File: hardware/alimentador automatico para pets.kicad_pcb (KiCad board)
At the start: 2 copper layers, 1 part, among them U1 ESP32-DEVKIT-V1

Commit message: pcb design start
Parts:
- added C1: 100n, Capacitor_THT:C_Disc_D6.0mm_W2.5mm_P5.00mm, F.Cu at (94.5, 80.0)
- added C2: 220u, Capacitor_THT:CP_Radial_D8.0mm_P2.50mm, F.Cu at (93.0, 71.0)
- added D1: LED, LED_THT:LED_D3.0mm, B.Cu at (92.0, 99.5)
- added D2: 3V6, Diode_THT:D_DO-35_SOD27_P7.62mm_Horizontal, B.Cu at (111.8, 40.4)
- added J1: Conn_01x02, Connector_PinSocket_2.54mm:PinSocket_1x02_P2.54mm_Vertical, F.Cu at (78.0, 47.0)
- added J2: Conn_01x04, Connector_PinSocket_2.54mm:PinSocket_1x04_P2.54mm_Vertical, F.Cu at (134.6, 77.2)
- added J3: Conn_01x03, Connector_PinSocket_2.54mm:PinSocket_1x03_P2.54mm_Vertical, F.Cu at (95.0, 92.0)
- added J4: Conn_01x03, Connector_PinSocket_2.54mm:PinSocket_1x03_P2.54mm_Vertical, F.Cu at (78.0, 82.0)
- added J5: Conn_01x02, Connector_PinSocket_2.54mm:PinSocket_1x02_P2.54mm_Vertical, F.Cu at (78.0, 38.0)
- added J6: Conn_01x05, Connector_PinSocket_2.54mm:PinSocket_1x05_P2.54mm_Vertical, F.Cu at (138.8, 35.4)
- added J7: Conn_01x02, Connector_PinSocket_2.54mm:PinSocket_1x02_P2.54mm_Vertical, F.Cu at (139.0, 66.0)
- added J8: Conn_01x04, Connector_PinSocket_2.54mm:PinSocket_1x04_P2.54mm_Vertical, F.Cu at (139.0, 51.9)
- added PS1: HLK-PM01 5V, Converter_ACDC:Converter_ACDC_HiLink_HLK-PMxx, F.Cu at (94.5, 32.4)
- added R1: 10k, Resistor_THT:R_Axial_DIN0207_L6.3mm_D2.5mm_P7.62mm_Horizontal, F.Cu at (82.2, 87.0)
- added R2: 10k, Resistor_THT:R_Axial_DIN0207_L6.3mm_D2.5mm_P7.62mm_Horizontal, F.Cu at (85.8, 71.0)
- added R3: 4k7, Resistor_THT:R_Axial_DIN0207_L6.3mm_D2.5mm_P7.62mm_Horizontal, F.Cu at (78.0, 68.0)
- added R4: 470, Resistor_THT:R_Axial_DIN0207_L6.3mm_D2.5mm_P7.62mm_Horizontal, B.Cu at (78.0, 87.2)
- added R5: 470, Resistor_THT:R_Axial_DIN0207_L6.3mm_D2.5mm_P7.62mm_Horizontal, B.Cu at (125.8, 58.4)
- added R6: 10k, Resistor_THT:R_Axial_DIN0207_L6.3mm_D2.5mm_P7.62mm_Horizontal, F.Cu at (90.0, 92.0)
- added SW1: SW_Push, Button_Switch_THT:SW_PUSH_6mm, B.Cu at (118.8, 97.8)
- added SW2: SW_Push, Button_Switch_THT:SW_PUSH_6mm, B.Cu at (130.8, 97.5)
- added SW3: SW_Push, Button_Switch_THT:SW_PUSH_6mm, B.Cu at (106.2, 97.5)
- added U2: HX711_module, footprint_lib:HX711_module, F.Cu at (114.2, 83.2)
- moved U1 49.5 mm to (119.4, 46.0)
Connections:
- net Net-(U1-Pad2) renamed GND
- U1 pad 1: unconnected-(U1-Pad1) -> /3V3
- U1 pad 10: unconnected-(U1-Pad10) -> /sMotor
- U1 pad 11: unconnected-(U1-Pad11) -> /SDA_disp
- U1 pad 14: unconnected-(U1-Pad14) -> /SCL_disp
- U1 pad 19: unconnected-(U1-Pad19) -> /led_on
- U1 pad 21: unconnected-(U1-Pad21) -> /BUTTON_1
- U1 pad 22: unconnected-(U1-Pad22) -> /BUTTON_2
- U1 pad 23: unconnected-(U1-Pad23) -> /BUTTON_3
- U1 pad 25: unconnected-(U1-Pad25) -> /SCK
- U1 pad 26: unconnected-(U1-Pad26) -> /DT_encoder
- U1 pad 27: unconnected-(U1-Pad27) -> /DT
- U1 pad 28: unconnected-(U1-Pad28) -> /SW_encoder
- U1 pad 3: unconnected-(U1-Pad3) -> /CLK_encoder
- U1 pad 30: unconnected-(U1-Pad30) -> /5V
- U1 pad 5: unconnected-(U1-Pad5) -> /IR_out
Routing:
- net GND: vias 0 -> 4
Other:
- board outline added: 69.5 x 88 mm

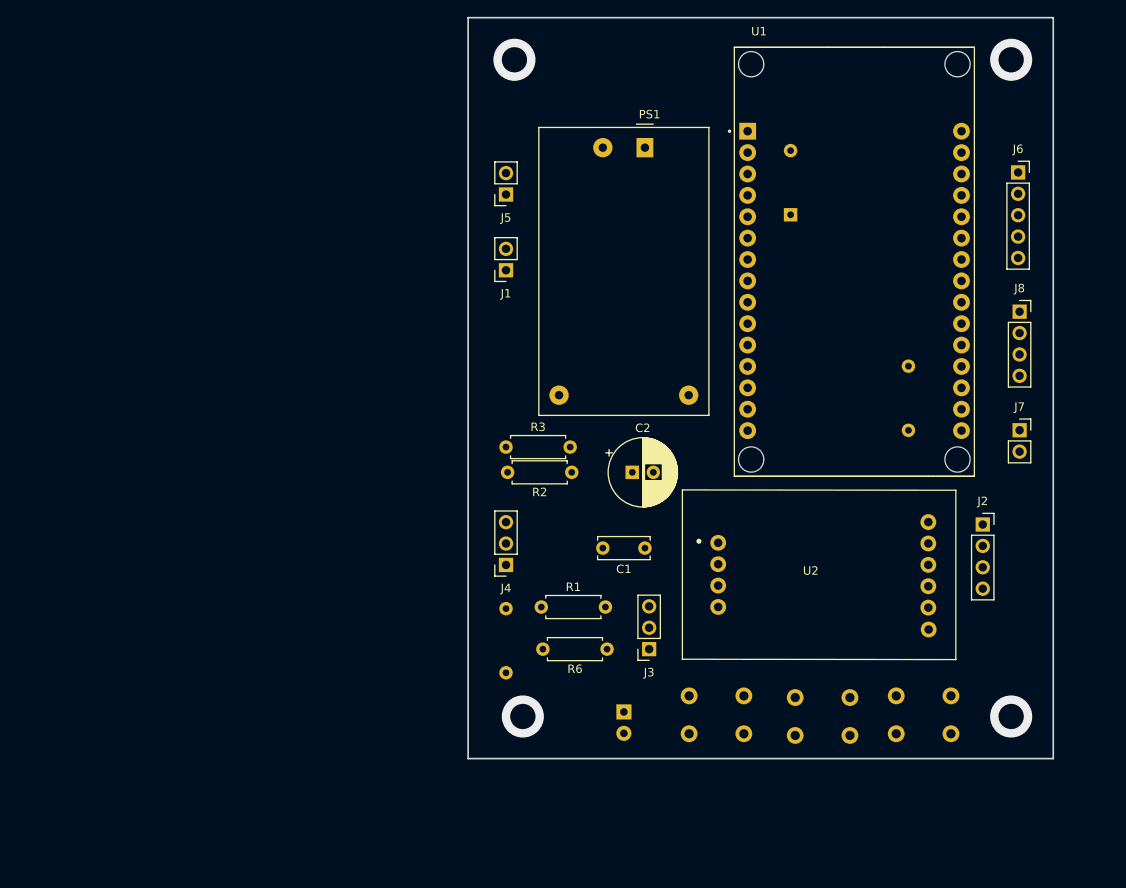
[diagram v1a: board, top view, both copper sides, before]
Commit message: removing leds and changing components positions #14
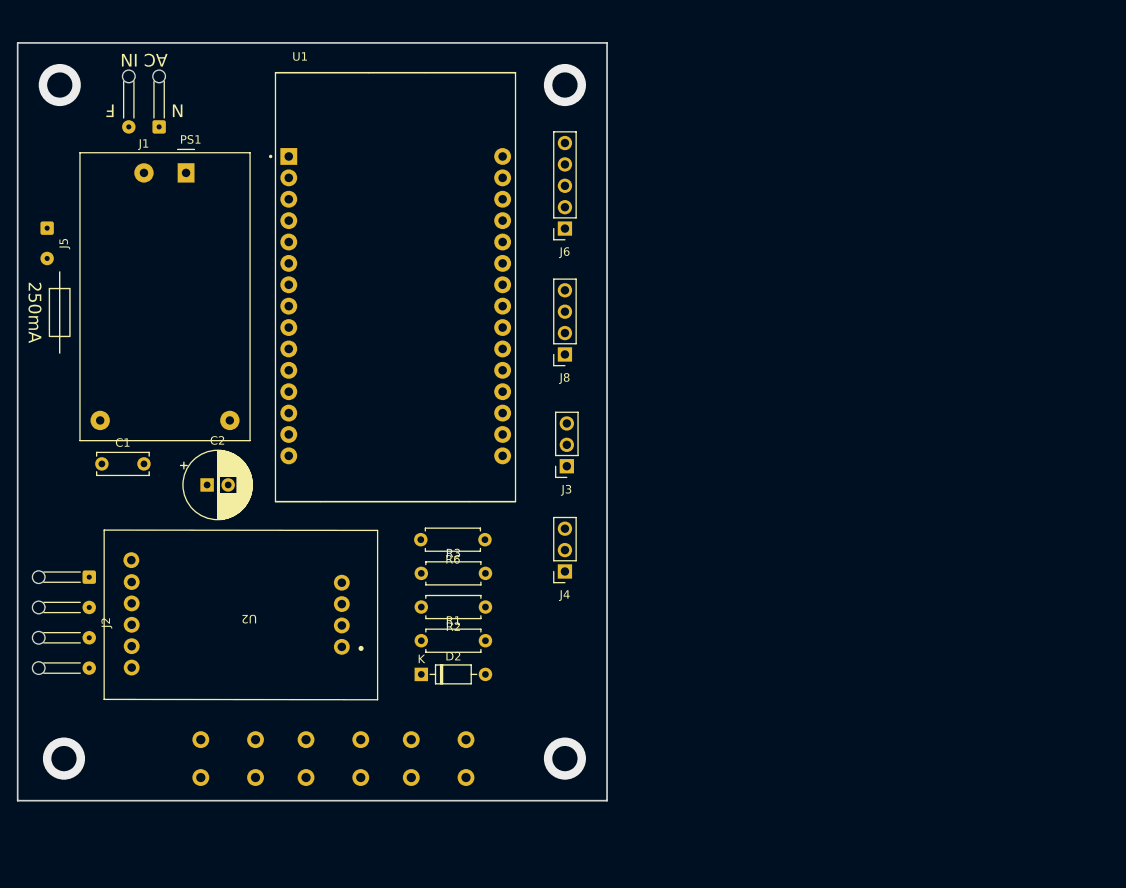
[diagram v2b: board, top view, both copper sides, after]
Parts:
- removed D1: LED, LED_THT:LED_D3.0mm
- removed J7: Conn_01x02, Connector_PinSocket_2.54mm:PinSocket_1x02_P2.54mm_Vertical
- removed R4, R5: 470, Resistor_THT:R_Axial_DIN0207_L6.3mm_D2.5mm_P7.62mm_Horizontal
- added G***: LOGO, footprint_lib:fuse_ieee, F.Cu at (25.0, 52.0)
- D2: moved to F.Cu
- J1: footprint Connector_PinSocket_2.54mm:PinSocket_1x02_P2.54mm_Vertical -> Connector_Wire:SolderWire-0.1sqmm_1x02_P3.6mm_D0.4mm_OD1mm_Relief
- J2: footprint Connector_PinSocket_2.54mm:PinSocket_1x04_P2.54mm_Vertical -> Connector_Wire:SolderWire-0.1sqmm_1x04_P3.6mm_D0.4mm_OD1mm_Relief
- J5: footprint Connector_PinSocket_2.54mm:PinSocket_1x02_P2.54mm_Vertical -> Connector_Wire:SolderWire-0.1sqmm_1x02_P3.6mm_D0.4mm_OD1mm
- moved J2 106.3 mm to (28.5, 83.5), turned to -90 degrees
- moved D2 70.0 mm to (67.9, 95.0), turned to 0 degrees
- moved U2 66.9 mm to (47.5, 87.9), turned to 180 degrees
- moved C1 65.3 mm to (30.0, 70.0), turned to 0 degrees
- moved SW1 58.3 mm to (60.8, 102.8)
- moved SW3 58.2 mm to (48.2, 102.8)
- moved SW2 57.8 mm to (73.2, 102.8)
- moved J5 54.6 mm to (23.5, 42.0), turned to -90 degrees
- moved PS1 54.6 mm to (40.0, 35.4)
- moved U1 54.6 mm to (64.9, 49.0)
- moved J8 54.2 mm to (85.0, 57.0), turned to 180 degrees
- moved J6 54.2 mm to (85.0, 42.0), turned to 180 degrees
- moved C2 50.5 mm to (42.5, 72.5)
- moved J1 44.6 mm to (36.8, 30.0)
- moved J3 23.8 mm to (85.2, 70.3)
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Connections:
- J2 pad 1: /red_wire -> /green_wire
- J2 pad 2: /black_wire -> /white_wire
- J2 pad 3: /white_wire -> /black_wire
- J2 pad 4: /green_wire -> /red_wire
- J3 pad 2: /5V -> GND
- J3 pad 3: GND -> /5V
- J6 pad 1: /CLK_encoder -> GND
- J6 pad 2: /DT_encoder -> /3V3
- J6 pad 4: /3V3 -> /DT_encoder
- J6 pad 5: GND -> /CLK_encoder
- J8 pad 1: /SCL_disp -> GND
- J8 pad 2: /SDA_disp -> /5V
- J8 pad 3: /5V -> /SDA_disp
- J8 pad 4: GND -> /SCL_disp
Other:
- board size 69.5 x 88 mm -> 70 x 90 mm
- board text added: "250mA"
- board text added: "AC IN"
- board text added: "F"
- board text added: "N"

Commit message: add battery module
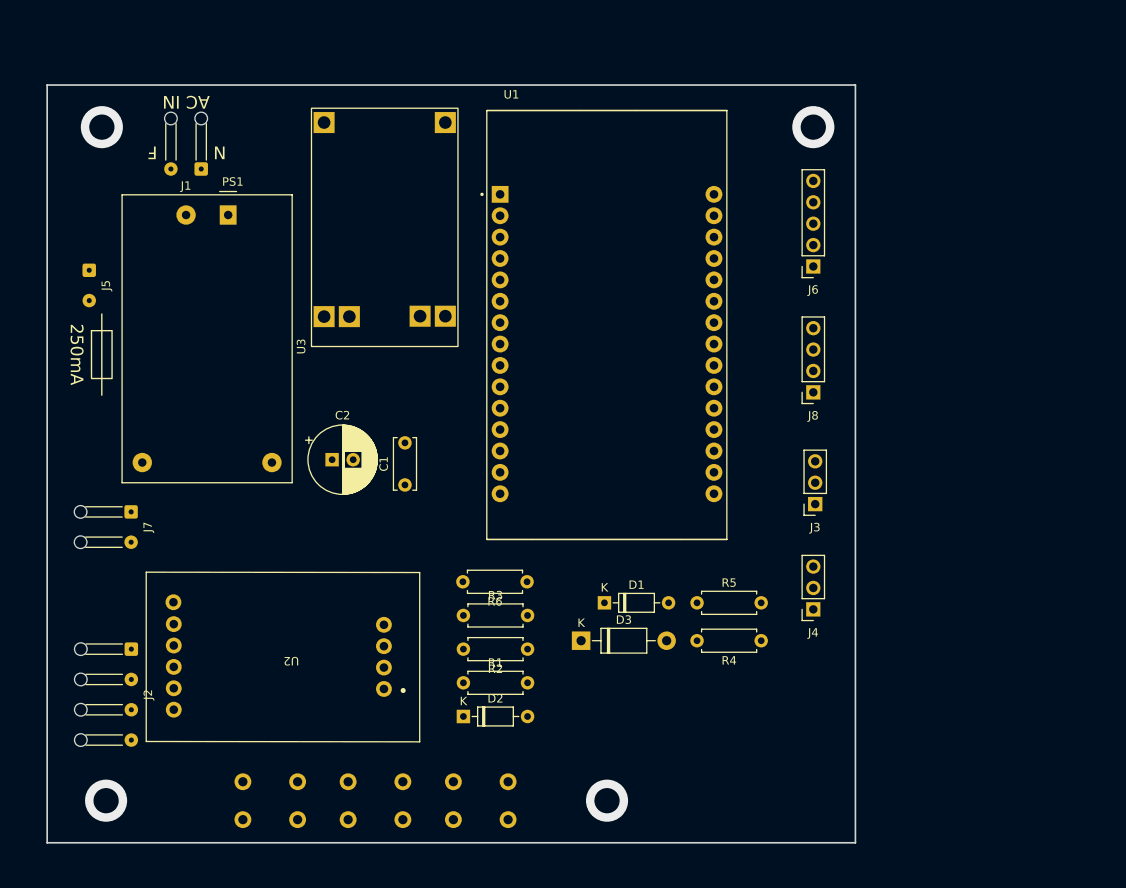
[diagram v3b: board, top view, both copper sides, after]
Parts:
- added D1: 3V6, Diode_THT:D_DO-35_SOD27_P7.62mm_Horizontal, F.Cu at (89.7, 86.5)
- added D3: 1N4007, Diode_THT:D_DO-41_SOD81_P10.16mm_Horizontal, F.Cu at (86.9, 91.0)
- added J7: Conn_01x02, Connector_Wire:SolderWire-0.1sqmm_1x02_P3.6mm_D0.4mm_OD1mm_Relief, F.Cu at (33.5, 75.7)
- added R4: 10k, Resistor_THT:R_Axial_DIN0207_L6.3mm_D2.5mm_P7.62mm_Horizontal, F.Cu at (108.3, 91.0)
- added R5: 10k, Resistor_THT:R_Axial_DIN0207_L6.3mm_D2.5mm_P7.62mm_Horizontal, F.Cu at (100.7, 86.5)
- added U3: TP4056, footprint_lib:TP4056, F.Cu at (54.9, 56.1)
- R3: value 4k7 -> 10k
- moved C1 36.1 mm to (66.0, 72.5), turned to 90 degrees
- moved J3 29.8 mm to (114.7, 74.8)
- moved J4 29.8 mm to (114.5, 87.3)
- moved J6 29.8 mm to (114.5, 46.5)
- moved J8 29.8 mm to (114.5, 61.5)
- moved U1 25.5 mm to (90.0, 53.5)
- moved C2 15.1 mm to (57.3, 69.5)
- moved J2 9.90 mm to (33.5, 92.0)
- moved D2 7.07 mm to (72.9, 100.0)
- moved G*** 7.07 mm to (30.0, 57.0)
- moved J1 7.07 mm to (41.8, 35.0)
- moved J5 7.07 mm to (28.5, 47.0)
- moved PS1 7.07 mm to (45.0, 40.4)
- moved R1 7.07 mm to (72.9, 96.0)
- moved R2 7.07 mm to (80.6, 92.0)
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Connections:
- R2 pad 2: Net-(R2-Pad2) -> Net-(R1-Pad2)
- R3 pad 1: Net-(R2-Pad2) -> /5V
- R3 pad 2: Net-(R1-Pad2) -> Net-(R3-Pad2)
- U1 pad 24: unconnected-(U1-Pad24) -> /ac_check
- U1 pad 30: /5V -> /+Vcc
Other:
- board size 70 x 90 mm -> 96 x 90 mm

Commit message: att schematic #14
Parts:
- J4: footprint Connector_PinSocket_2.54mm:PinSocket_1x03_P2.54mm_Vertical -> Connector_PinHeader_2.54mm:PinHeader_1x03_P2.54mm_Vertical
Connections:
- J4 pad 1: /5V -> /sMotor
- J4 pad 2: /sMotor -> /5V
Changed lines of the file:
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@@
     )
   )
-  (footprint "Connector_PinSocket_2.54mm:PinSocket_1x03_P2.54mm_Vertical" (layer "F.Cu")
+  (footprint "Connector_PinHeader_2.54mm:PinHeader_1x03_P2.54mm_Vertical" (layer "F.Cu")
     (at 114.5 87.275 180)
-    (descr "Through hole straight socket strip, 1x03, 2.54mm pitch, single row (from Kicad 4.0.7), script generated")
-    (tags "Through hole socket strip THT 1x03 2.54mm single row")
+    (descr "Through hole straight pin header, 1x03, 2.54mm pitch, single row")
+    (tags "Through hole pin header THT 1x03 2.54mm single row")
     (property "Sheetfile" "alimentador automatico para pets.kicad_sch")
     (property "Sheetname" "")
     (attr through_hole)
-    (fp_text reference "J4" (at 0 -2.77 180) (layer "F.SilkS")
+    (fp_text reference "J4" (at 0 -2.33 180) (layer "F.SilkS")
       (effects (font (size 1 1) (thickness 0.15)))
     )
-    (fp_text value "Conn_01x03" (at 0 7.85 180) (layer "F.Fab")
+    (fp_text value "Conn_01x03" (at 0 7.41 180) (layer "F.Fab")
       (effects (font (size 1 1) (thickness 0.15)))
     )
@@
     )
     (fp_line (start 1.33 1.27) (end 1.33 6.41) (layer "F.SilkS") (width 0.12))
-    (fp_line (start 0 -1.33) (end 1.33 -1.33) (layer "F.SilkS") (width 0.12))
+    (fp_line (start -1.33 0) (end -1.33 -1.33) (layer "F.SilkS") (width 0.12))
+    (fp_line (start -1.33 6.41) (end 1.33 6.41) (layer "F.SilkS") (width 0.12))
     (fp_line (start -1.33 1.27) (end 1.33 1.27) (layer "F.SilkS") (width 0.12))
-    (fp_line (start -1.33 6.41) (end 1.33 6.41) (layer "F.SilkS") (width 0.12))
+    (fp_line (start -1.33 -1.33) (end 0 -1.33) (layer "F.SilkS") (width 0.12))
     (fp_line (start -1.33 1.27) (end -1.33 6.41) (layer "F.SilkS") (width 0.12))
-    (fp_line (start 1.33 -1.33) (end 1.33 0) (layer "F.SilkS") (width 0.12))
-    (fp_line (start 1.75 6.85) (end -1.8 6.85) (layer "F.CrtYd") (width 0.05))
-    (fp_line (start -1.8 -1.8) (end 1.75 -1.8) (layer "F.CrtYd") (width 0.05))
-    (fp_line (start 1.75 -1.8) (end 1.75 6.85) (layer "F.CrtYd") (width 0.05))
-    (fp_line (start -1.8 6.85) (end -1.8 -1.8) (layer "F.CrtYd") (width 0.05))
-    (fp_line (start -1.27 -1.27) (end 0.635 -1.27) (layer "F.Fab") (width 0.1))
+    (fp_line (start -1.8 -1.8) (end -1.8 6.85) (layer "F.CrtYd") (width 0.05))
+    (fp_line (start 1.8 6.85) (end 1.8 -1.8) (layer "F.CrtYd") (width 0.05))
+    (fp_line (start 1.8 -1.8) (end -1.8 -1.8) (layer "F.CrtYd") (width 0.05))
+    (fp_line (start -1.8 6.85) (end 1.8 6.85) (layer "F.CrtYd") (width 0.05))
+    (fp_line (start 1.27 -1.27) (end 1.27 6.35) (layer "F.Fab") (width 0.1))
     (fp_line (start 1.27 6.35) (end -1.27 6.35) (layer "F.Fab") (width 0.1))
-    (fp_line (start -1.27 6.35) (end -1.27 -1.27) (layer "F.Fab") (width 0.1))
-    (fp_line (start 1.27 -0.635) (end 1.27 6.35) (layer "F.Fab") (width 0.1))
-    (fp_line (start 0.635 -1.27) (end 1.27 -0.635) (layer "F.Fab") (width 0.1))
+    (fp_line (start -1.27 -0.635) (end -0.635 -1.27) (layer "F.Fab") (width 0.1))
+    (fp_line (start -1.27 6.35) (end -1.27 -0.635) (layer "F.Fab") (width 0.1))
+    (fp_line (start -0.635 -1.27) (end 1.27 -1.27) (layer "F.Fab") (width 0.1))
     (pad "1" thru_hole rect (at 0 0 180) (size 1.7 1.7) (drill 1) (layers *.Cu *.Mask)
-      (net 1 "/5V") (pinfunction "Pin_1") (pintype "passive"))
+      (net 23 "/sMotor") (pinfunction "Pin_1") (pintype "passive"))
     (pad "2" thru_hole oval (at 0 2.54 180) (size 1.7 1.7) (drill 1) (layers *.Cu *.Mask)
-      (net 23 "/sMotor") (pinfunction "Pin_2") (pintype "passive"))
+      (net 1 "/5V") (pinfunction "Pin_2") (pintype "passive"))
     (pad "3" thru_hole oval (at 0 5.08 180) (size 1.7 1.7) (drill 1) (layers *.Cu *.Mask)
       (net 2 "GND") (pinfunction "Pin_3") (pintype "passive"))
-    (model "${KICAD6_3DMODEL_DIR}/Connector_PinSocket_2.54mm.3dshapes/PinSocket_1x03_P2.54mm_Vertical.wrl"
+    (model "${KICAD6_3DMODEL_DIR}/Connector_PinHeader_2.54mm.3dshapes/PinHeader_1x03_P2.54mm_Vertical.wrl"
       (offset (xyz 0 0 0))
       (scale (xyz 1 1 1))

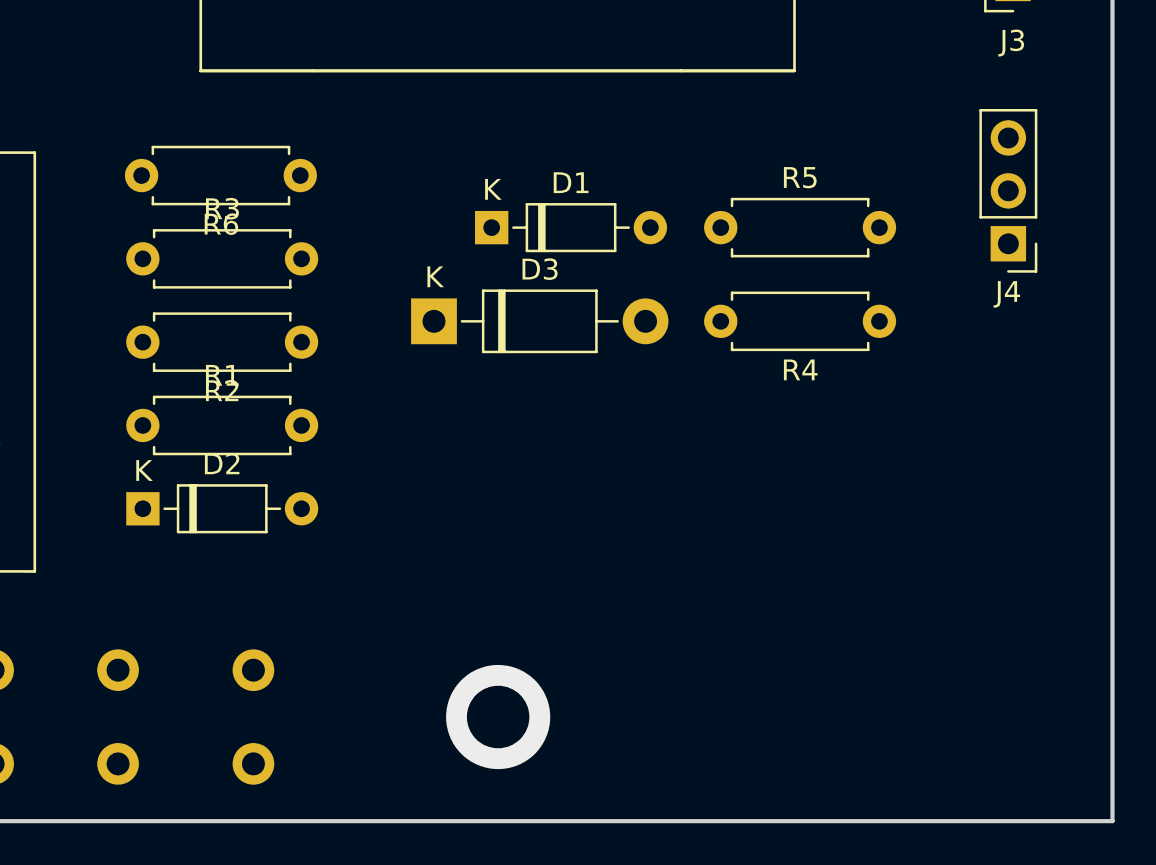
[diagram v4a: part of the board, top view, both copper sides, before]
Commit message: added buzzer #21
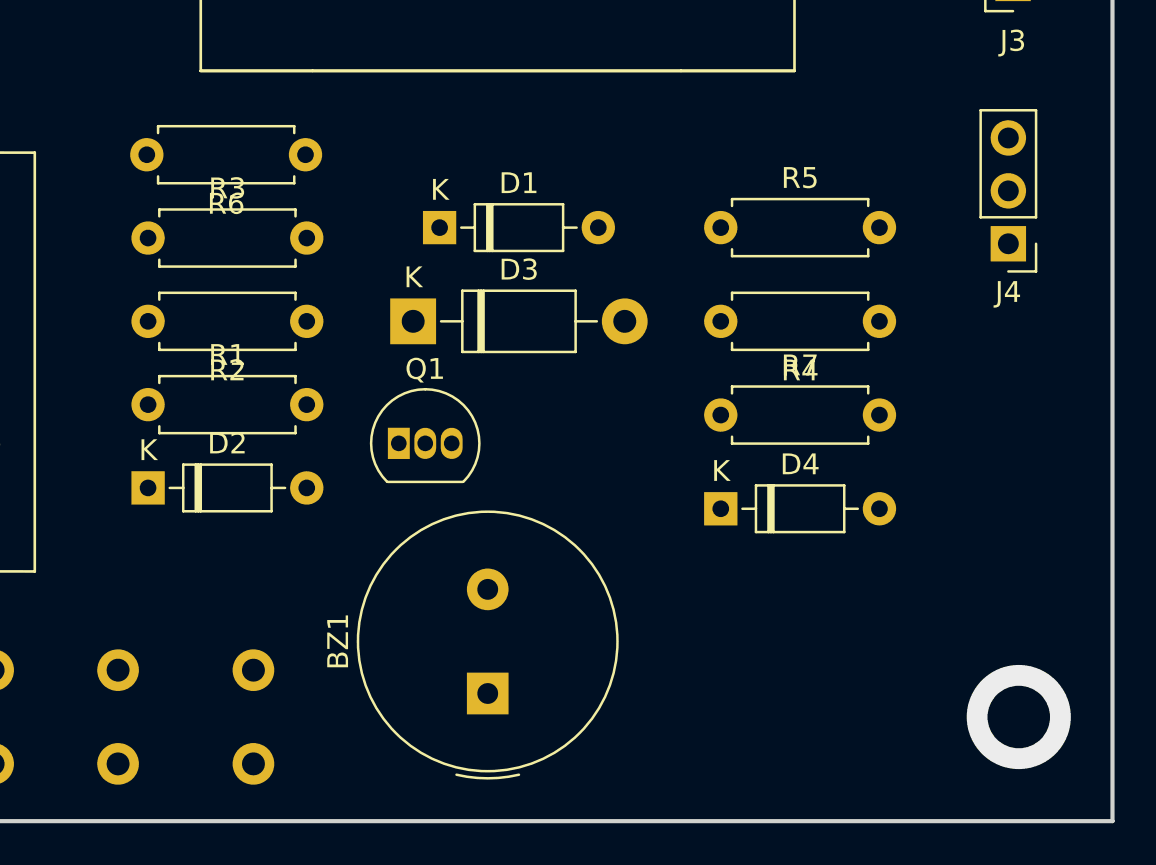
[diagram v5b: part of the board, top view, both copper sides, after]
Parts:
- added BZ1: Buzzer, Buzzer_Beeper:Buzzer_TDK_PS1240P02BT_D12.2mm_H6.5mm, F.Cu at (89.5, 108.9)
- added D4: 1N4148, Diode_THT:D_DO-35_SOD27_P7.62mm_Horizontal, F.Cu at (100.7, 100.0)
- added Q1: BC337, Package_TO_SOT_THT:TO-92_Inline, F.Cu at (85.2, 96.9)
- added R7: 1k, Resistor_THT:R_Axial_DIN0207_L6.3mm_D2.5mm_P7.62mm_Horizontal, F.Cu at (100.7, 95.5)
- moved D1 2.50 mm to (87.2, 86.5)
- moved D2 1.03 mm to (73.2, 99.0)
- moved R1 1.03 mm to (73.2, 95.0)
- moved R2 1.03 mm to (80.8, 91.0)
- moved R3 1.03 mm to (73.2, 87.0)
- moved R6 1.03 mm to (80.8, 83.0)
- moved D3 1.00 mm to (85.9, 91.0)
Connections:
- U1 pad 9: unconnected-(U1-Pad9) -> /buzzer
